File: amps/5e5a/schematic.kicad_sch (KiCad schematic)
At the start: 60 parts, among them T2 ~4.3k:8

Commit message: Fix: draw the 1 MΩ input grid leak on the jack-1 tip node, not the grid, on eight tweed/Champ sheets
Every tweed and Champ factory sheet hangs the 1 MΩ from the jack-1 tip
node (the node the jack-2 shorting contact also lands on) to ground, and
runs the 68 K stoppers from the jack tips to the grid. These eight sheets
drew the 1 MΩ on the GRID side of the stopper — one copy-pasted idiom in
four scripts and its cousins in four more; there is no shared helper, so
each script is fixed where it draws the block. The stopper is declared
DC-transparent (layout net_map.series_bridge), so the netlist sees one node
either way and verify_schematic_nets stays 40 clean; the sheet-vs-board
gate, which compares the drawings to each other, drops all twelve
MISPLACED findings (RG1/RG2 on 5e4a, 5e5a, 5f4, 5f6; R3 on 5f2a, aa764,
aa764-vibro; R1 on 5f1). 5f10's jack chain is a separate task.

Crops read: 5e4a-RG1-RG2-input.png, 5e5a-RG1-RG2-input.png,
5f4-RG1-input.png, 5f6-RG1-RG2-input.png, 5f2a-R3-input.png,
5f1-R1-input.png, aa764-R3-input.png, aa764-vibro-R3-input.png — each
prints "1 MEG." from the jack-1 tip to ground with the 68K pair to the grid.

Geometry: the four two-channel sheets hang the leak from the stopper's
jack-side pin; 5f1 drops it from the INPUT line; 5f2a and the two Champs
stand it upward off the jack-1 line because the jack-2 line runs 8–12 mm
below. Previews read cleanly. The circuit stories already say the leaks
mount at the jacks, so no prose changed.

Gates: check_schematics 40/0 (0 isolated), verify_schematic_nets 40
clean, validate/value-consistency/era-values clean, regenerate-all leaves
every other sheet byte-identical. verify_sheet_vs_board misplaced 98 -> 86.

Co-Authored-By: Claude Fable 5.1 <noreply@anthropic.com>
Claude-Session: https://claude.ai/code/session_01KBMfdh37HmCL2iWcBiL5J1
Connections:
- net INST: now also RG1.1
- net MIC: now also RG2.1
- net at R1s.2, V1A.2 (G): no longer RG1.1
- net at R2s.2, V1B.2 (G): no longer RG2.1
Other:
- moved on the sheet: RG1, RG2
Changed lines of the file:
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@@
   (wire (pts (xy 30.3 53.7) (xy 34.11 53.7))
     (stroke (width 0) (type default)))
-  (junction (at 30.3 53.7) (diameter 1.151) (color 0 0 0 0))
-  (symbol (lib_id "cx:R") (at 30.3 57.51 0) (unit 1)
+  (junction (at 22.68 53.7) (diameter 1.151) (color 0 0 0 0))
+  (symbol (lib_id "cx:R") (at 22.68 57.51 0) (unit 1)
     (in_bom yes) (on_board yes)
-    (property "Reference" "RG1" (at 32.5 54.31 0) (effects (font (size 1.27 1.27)) (justify left)))
-    (property "Value" "1M" (at 32.5 56.71 0) (effects (font (size 1.27 1.27)) (justify left))))
-  (global_label "GND" (shape input) (at 30.3 61.32 270)
+    (property "Reference" "RG1" (at 24.88 57.51 0) (effects (font (size 1.27 1.27)) (justify left)))
+    (property "Value" "1M" (at 24.88 59.91 0) (effects (font (size 1.27 1.27)) (justify left))))
+  (global_label "GND" (shape input) (at 22.68 61.32 270)
     (effects (font (size 1.27 1.27)) (justify right)))
   (wire (pts (xy 41.73 46.08) (xy 41.73 42.6))
@@
   (wire (pts (xy 30.3 87.7) (xy 34.11 87.7))
     (stroke (width 0) (type default)))
-  (junction (at 30.3 87.7) (diameter 1.151) (color 0 0 0 0))
-  (symbol (lib_id "cx:R") (at 30.3 91.51 0) (unit 1)
+  (junction (at 22.68 87.7) (diameter 1.151) (color 0 0 0 0))
+  (symbol (lib_id "cx:R") (at 22.68 91.51 0) (unit 1)
     (in_bom yes) (on_board yes)
-    (property "Reference" "RG2" (at 32.5 88.31 0) (effects (font (size 1.27 1.27)) (justify left)))
-    (property "Value" "1M" (at 32.5 90.71 0) (effects (font (size 1.27 1.27)) (justify left))))
-  (global_label "GND" (shape input) (at 30.3 95.32 270)
+    (property "Reference" "RG2" (at 24.88 91.51 0) (effects (font (size 1.27 1.27)) (justify left)))
+    (property "Value" "1M" (at 24.88 93.91 0) (effects (font (size 1.27 1.27)) (justify left))))
+  (global_label "GND" (shape input) (at 22.68 95.32 270)
     (effects (font (size 1.27 1.27)) (justify right)))
   (wire (pts (xy 41.73 80.08) (xy 41.73 76.6))

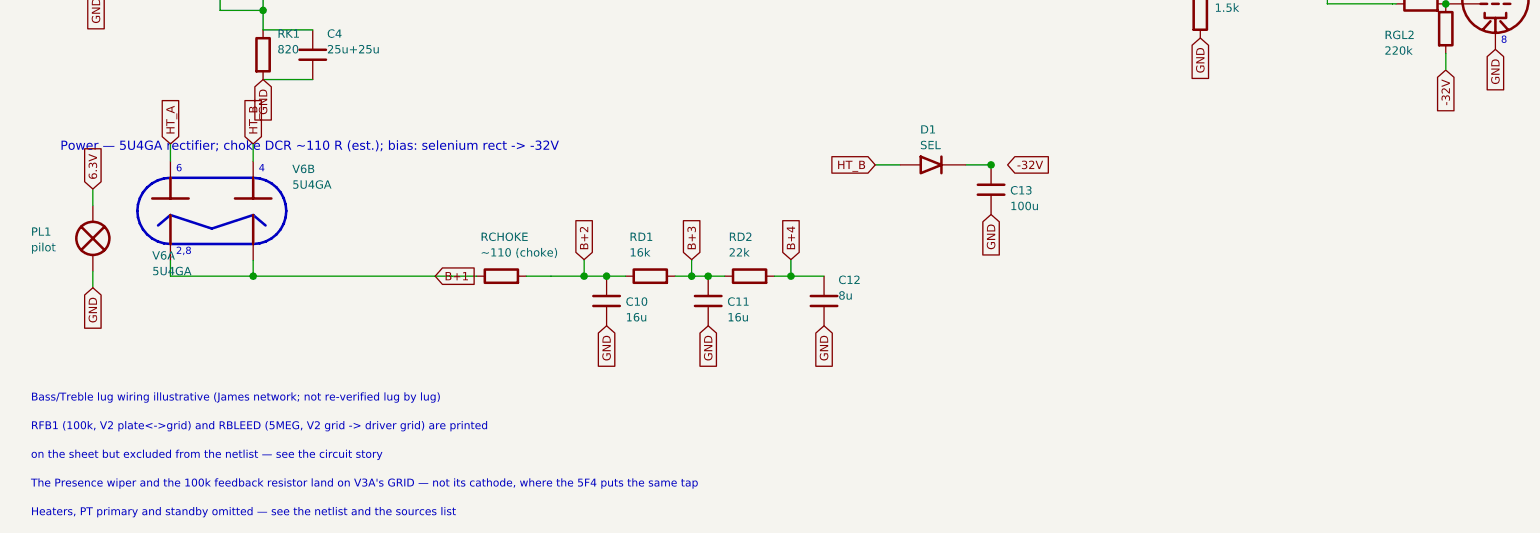
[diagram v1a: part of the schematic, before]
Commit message: Fix: feed the tweed bias rectifiers from the transformer's bias tap, not a rectifier plate (5E4-A, 5E5-A, 5F4, 5G9)
The 8087-family power transformer brings out a BIAS TAP on the HT winding,
between one end and the centre tap — the layouts letter that lead RED-BLUE
— and every fixed-bias tweed factory sheet draws the bias rectifier from
that fourth winding terminal. These four sheets drew it from a rectifier
plate (the HT_B label). The boards carry the same mistake, which is why the
sheet-vs-board gate could not see it; the source read did.

cx:PT gains an OPTIONAL pin 6, HT_TAP, between HT_A and the centre tap.
`s.pt(..., tap=True)` asks for it, and only that sheet's embedded library
carries the pin (lib_text(pt_tap=...)), so every sheet that does not wire
it is byte-identical — proved by the regenerate-all diff below. The
contract tables (SYM_EXTENTS/SYM_PINS) are built with the pin so the lint
and the wire-cutting know it; the tap lies inside the symbol's box, so no
extent moves.

- 5g9: T1 8160 drawn with the tap (moved 8 mm left for the label), the
  selenium rectifier's AC side on HT_TAP (crop 5g9-D1-schem.png: the
  rectifier + runs straight to a winding terminal between the 300 V AC end
  and the centre tap; layout: a separate lead to SEL. RECT. +).
- 5e4a, 5f4: these sheets drew no PT at all, so a T1 is added (MAINS labels
  on the primary, HT_A / HT_TAP / centre tap / HT_B on the secondary, the
  same idiom the 5G9 uses), the 18k / 6800 bias feed taken from HT_TAP,
  and T1 added to bom.yaml (crops 5e4a-D1-schem.png, 5f4-D1-schem.png:
  the series resistor from a winding terminal between the top end and the
  centre tap; 5e4a-D1-layout.png: RED-BLUE lead to the selenium +).
- 5e5a: T1 added the same way; the bias row now carries the factory's 10 K
  in series from the tap into the cell and the 56 K bleeder across the
  100 µF can (crop 5e5a-D1-schem.png), both added to bom.yaml (RB1, RB2)
  — the board places neither, so they report SHEET-ONLY until it doe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
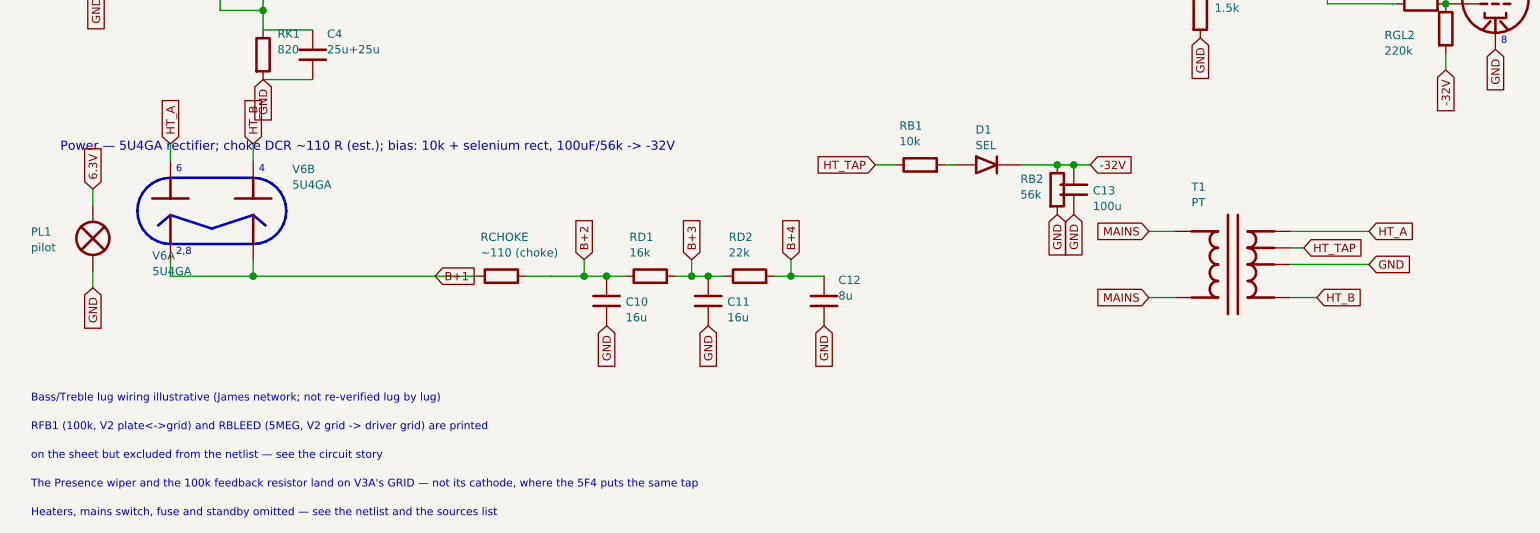
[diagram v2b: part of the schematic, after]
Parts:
- added RB1: 10k, symbol cx:R
- added RB2: 56k, symbol cx:R
- added T1: PT, symbol cx:PT
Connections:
- net -32V: now also C13.1, D1.2 (K), RB2.1
- net GND: now also RB2.2, T1.4 (HT_CT)
- net HT_A: now also T1.3 (HT_A)
- net HT_B: now also T1.5 (HT_B); no longer D1.1 (A)
- new net: D1.1 (A), RB1.2
- new net HT_TAP: RB1.1, T1.6 (HT_TAP)
- new net MAINS: T1.1 (PRI_1), T1.2 (PRI_2)
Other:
- note added: "Heaters, mains switch, fuse and standby omitted — see the netlist and the sources list"
- note added: "Power — 5U4GA rectifier; choke DCR ~110 R (est.); bias: 10k + selenium rect, 100uF/56k -> -32V"
- note removed: "Heaters, PT primary and standby omitted — see the netlist and the sources list"
- note removed: "Power — 5U4GA rectifier; choke DCR ~110 R (est.); bias: selenium rect -> -32V"
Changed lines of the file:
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@@
   (text "Extra 8-ohm speaker jack (parallel) omitted — annotation only" (at 242.2 83.7 0)
     (effects (font (size 1 1)) (justify left)))
-  (text "Power — 5U4GA rectifier; choke DCR ~110 R (est.); bias: selenium rect -> -32V" (at 17.2 119.7 0)
+  (text "Power — 5U4GA rectifier; choke DCR ~110 R (est.); bias: 10k + selenium rect, 100uF/56k -> -32V" (at 17.2 119.7 0)
     (effects (font (size 1.4 1.4)) (justify left)))
   (symbol (lib_id "cx:LAMP") (at 22.2 133.7 0) (unit 1)
@@
   (global_label "GND" (shape input) (at 134.44 147.12 270)
     (effects (font (size 1.27 1.27)) (justify right)))
-  (global_label "HT_B" (shape input) (at 142.3 122.42 180)
-    (effects (font (size 1.27 1.27)) (justify right)))
-  (wire (pts (xy 142.3 122.42) (xy 146.11 122.42))
-    (stroke (width 0) (type default)))
-  (symbol (lib_id "cx:DIODE_SS") (at 151.19 122.42 0) (unit 1)
-    (in_bom yes) (on_board yes)
-    (property "Reference" "D1" (at 149.19 117.02 0) (effects (font (size 1.27 1.27)) (justify left)))
-    (property "Value" "SEL" (at 149.19 119.42 0) (effects (font (size 1.27 1.27)) (justify left))))
-  (wire (pts (xy 156.27 122.42) (xy 160.08 122.42))
-    (stroke (width 0) (type default)))
-  (junction (at 160.08 122.42) (diameter 1.151) (color 0 0 0 0))
-  (symbol (lib_id "cx:C") (at 160.08 126.23 0) (unit 1)
-    (in_bom yes) (on_board yes)
-    (property "Reference" "C13" (at 163.012 126.368 0) (effects (font (size 1.27 1.27)) (justify left)))
-    (property "Value" "100u" (at 163.012 128.768 0) (effects (font (size 1.27 1.27)) (justify left))))
-  (global_label "GND" (shape input) (at 160.08 130.04 270)
-    (effects (font (size 1.27 1.27)) (justify right)))
-  (global_label "-32V" (shape input) (at 162.62 122.42 0)
+  (global_label "HT_TAP" (shape input) (at 142.3 122.42 180)
+    (effects (font (size 1.27 1.27)) (justify right)))
+  (symbol (lib_id "cx:R") (at 149.2 122.42 90) (unit 1)
+    (in_bom yes) (on_board yes)
+    (property "Reference" "RB1" (at 146 116.42 270) (effects (font (size 1.27 1.27)) (justify left)))
+    (property "Value" "10k" (at 146 118.82 270) (effects (font (size 1.27 1.27)) (justify left))))
+  (wire (pts (xy 142.3 122.42) (xy 145.39 122.42))
+    (stroke (width 0) (type default)))
+  (wire (pts (xy 153.01 122.42) (xy 154.62 122.42))
+    (stroke (width 0) (type default)))
+  (symbol (lib_id "cx:DIODE_SS") (at 159.7 122.42 0) (unit 1)
+    (in_bom yes) (on_board yes)
+    (property "Reference" "D1" (at 157.7 117.02 0) (effects (font (size 1.27 1.27)) (justify left)))
+    (property "Value" "SEL" (at 157.7 119.42 0) (effects (font (size 1.27 1.27)) (justify left))))
+  (wire (pts (xy 164.78 122.42) (xy 170.24 122.42))
+    (stroke (width 0) (type default)))
+  (wire (pts (xy 170.24 122.42) (xy 172.78 122.42))
+    (stroke (width 0) (type default)))
+  (wire (pts (xy 172.78 122.42) (xy 175.32 122.42))
+    (stroke (width 0) (type default)))
+  (junction (at 170.24 122.42) (diameter 1.151) (color 0 0 0 0))
+  (symbol (lib_id "cx:R") (at 170.24 126.23 0) (unit 1)
+    (in_bom yes) (on_board yes)
+    (property "Reference" "RB2" (at 164.575 124.59 0) (effects (font (size 1.27 1.27)) (justify left)))
+    (property "Value" "56k" (at 164.575 126.99 0) (effects (font (size 1.27 1.27)) (justify left))))
+  (global_label "GND" (shape input) (at 170.24 130.04 270)
+    (effects (font (size 1.27 1.27)) (justify right)))
+  (junction (at 172.78 122.42) (diameter 1.151) (color 0 0 0 0))
+  (symbol (lib_id "cx:C") (at 172.78 126.23 0) (unit 1)
+    (in_bom yes) (on_board yes)
+    (property "Reference" "C13" (at 175.712 126.368 0) (effects (font (size 1.27 1.27)) (justify left)))
+    (property "Value" "100u" (at 175.712 128.768 0) (effects (font (size 1.27 1.27)) (justify left))))
+  (global_label "GND" (shape input) (at 172.78 130.04 270)
+    (effects (font (size 1.27 1.27)) (justify right)))
+  (global_label "-32V" (shape input) (at 175.32 122.42 0)
+    (effects (font (size 1.27 1.27)) (justify left)))
+  (symbol (lib_id "cx:PT") (at 197.2 137.7 0) (unit 1)
+    (in_bom yes) (on_board yes)
+    (property "Reference" "T1" (at 190.85 125.8 0) (effects (font (size 1.27 1.27)) (justify left)))
+    (property "Value" "PT" (at 190.85 128.2 0) (effects (font (size 1.27 1.27)) (justify left))))
+  (wire (pts (xy 188.31 132.62) (xy 184.31 132.62))
+    (stroke (width 0) (type default)))
+  (global_label "MAINS" (shape input) (at 184.31 132.62 180)
+    (effects (font (size 1.27 1.27)) (justify right)))
+  (wire (pts (xy 188.31 142.78) (xy 184.31 142.78))
+    (stroke (width 0) (type default)))
+  (global_label "MAINS" (shape input) (at 184.31 142.78 180)
+    (effects (font (size 1.27 1.27)) (justify right)))
+  (wire (pts (xy 206.09 132.62) (xy 218.09 132.62))
+    (stroke (width 0) (type default)))
+  (global_label "HT_A" (shape input) (at 218.09 132.62 0)
+    (effects (font (size 1.27 1.27)) (justify left)))
+  (wire (pts (xy 206.09 135.16) (xy 208.09 135.16))
+    (stroke (width 0) (type default)))
+  (global_label "HT_TAP" (shape input) (at 208.09 135.16 0)
+    (effects (font (size 1.27 1.27)) (justify left)))
+  (wire (pts (xy 206.09 137.7) (xy 218.09 137.7))
+    (stroke (width 0) (type default)))
+  (global_label "GND" (shape input) (at 218.09 137.7 0)
+    (effects (font (size 1.27 1.27)) (justify left)))
+  (wire (pts (xy 206.09 142.78) (xy 210.09 142.78))
+    (stroke (width 0) (type default)))
+  (global_label "HT_B" (shape input) (at 210.09 142.78 0)
     (effects (font (size 1.27 1.27)) (justify left)))
   (polyline (pts (xy 46.81 124.4) (xy 47.801 124.498) (xy 48.754 124.787) (xy 49.632 125.256) (xy 50.402 125.888) (xy 51.034 126.658) (xy 51.503 127.536) (xy 51.792 128.489) (xy 51.89 129.48) (xy 51.792 130.471) (xy 51.503 131.424) (xy 51.034 132.302) (xy 50.402 133.072) (xy 49.632 133.704) (xy 48.754 134.173) (xy 47.801 134.462) (xy 46.81 134.56) (xy 34.11 134.56) (xy 33.119 134.462) (xy 32.166 134.173) (xy 31.288 133.704) (xy 30.518 133.072) (xy 29.886 132.302) (xy 29.417 131.424) (xy 29.128 130.471) (xy 29.03 129.48) (xy 29.128 128.489) (xy 29.417 127.536) (xy 29.886 126.658) (xy 30.518 125.888) (xy 31.288 125.256) (xy 32.166 124.787) (xy 33.119 124.498) (xy 34.11 124.4) (xy 46.81 124.4))
@@
   (text "The Presence wiper and the 100k feedback resistor land on V3A's GRID — not its cathode, where the 5F4 puts the same tap" (at 12.7 171.478 0)
     (effects (font (size 1.2 1.2)) (justify left)))
-  (text "Heaters, PT primary and standby omitted — see the netlist and the sources list" (at 12.7 175.878 0)
+  (text "Heaters, mains switch, fuse and standby omitted — see the netlist and the sources list" (at 12.7 175.878 0)
     (effects (font (size 1.2 1.2)) (justify left)))
   (sheet_instances (path "/" (page "1")))

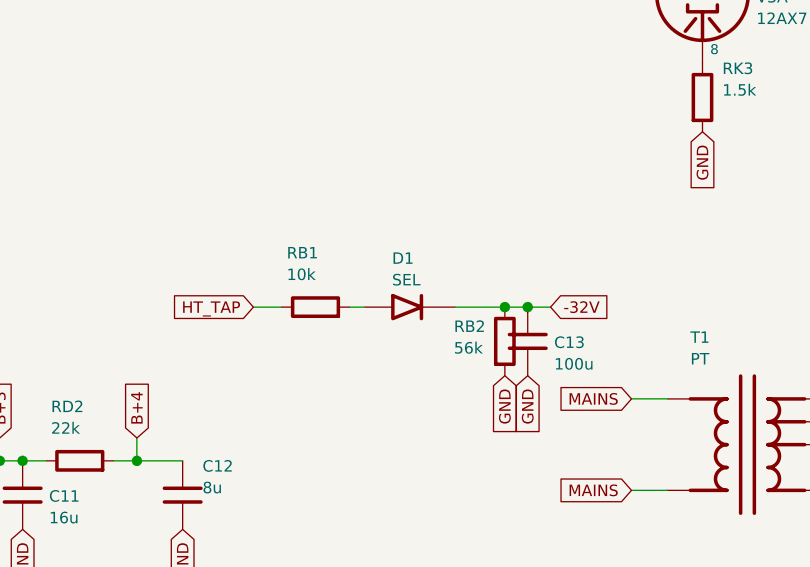
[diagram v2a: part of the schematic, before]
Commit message: Fix: 17 bias rectifiers and six HT diodes drawn backwards; the 6G6-B and 6G4 bias rows as their drawings show; AA1164 V4 units
Rectifier polarity has no gate. The netlists model every supply as an ideal
source, the sheet-vs-board check treats a two-terminal part as unordered, and
the boards' `cathode:` fields were copied from the sheets. Measured over all
68 diodes on 40 sheets: 18 negative-bias rectifiers had the cathode on the
negative node (a diode that way round would charge the node POSITIVE), and all
six 6G6-B HT diodes pointed away from B+. The printed negative bias on each of
those sheets falsifies the drawn orientation; the nine bias rectifiers already
right (AA1164, AA864, AB165, B15N, DR103, JTM100, M1959, M2204, 6G6-B) show
the idiom. Flipped: 5E4-A, 5E5-A, 5E6-A, 5F10, 5F4, 5F6, 5F6-A, 5F8-A, 5G9,
6G2, 6G3, 6G4, 6G5, AA964, AB763, AB763 Super, AB763 Twin, JTM45 (the
M1987's is with the Marshall board repair) and the 6G6-B's DR1-DR6. The
5F8-A board, which had copied its sheet, has the band moved to the tap side;
the other boards' bands are with the board-repair wave. A gate is next.

6G6-B bias. E-FB (6431x3364): the 1K 1W rises from TR1's SECOND secondary
terminal, a bias tap between the upper HT end and the grounded centre tap,
to the diode's + end. The sheet fed the diode from the HT end with the 1K
after it. T1 now carries its tap pin and the row reads tap -> 1K -> diode ->
-54 V. (The triage had read "HT end"; the native crop shows the tap.)

6G4 bias. A-FJ, read natively: tap -> rectifier -> 8 uF -> 10K -> the -55 V
node, which carries a second 8 uF and the 56K to ground as a bleeder. The
sheet fed the rectifier from an HT end, drew the 56K in series and carried
one capacitor. CBIAS2 joins the parts list, and RBIAS1's role now says
bleeder.

AA1164 V4. The K-FD sheet prints the phase inverter 7/6/8 and the tremolo
oscillator 2/1/3 (5554x4346); the sheet had them the other way round.

Gates: check_schematics 40/0 (+selftest), verify_schematic_nets 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
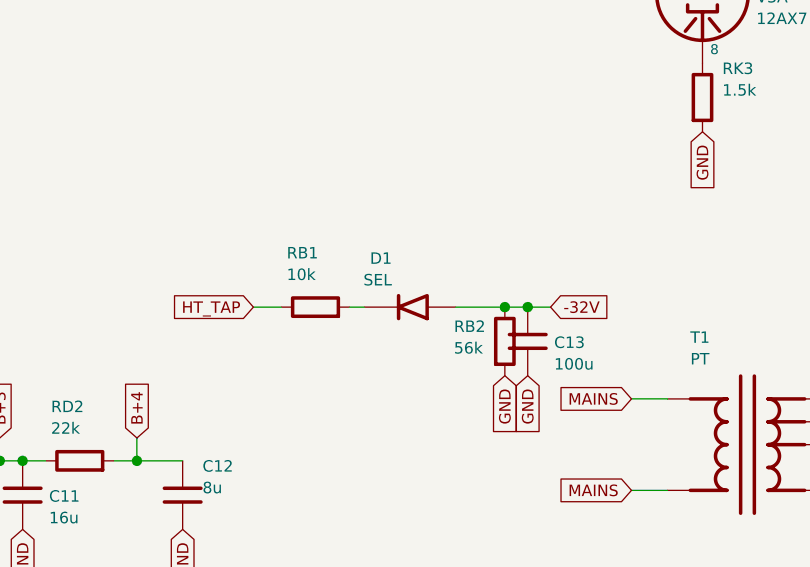
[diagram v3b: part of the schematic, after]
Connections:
- net -32V: now also D1.1 (A); no longer D1.2 (K)
- net at RB1.2: now also D1.2 (K); no longer D1.1 (A)
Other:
- moved on the sheet: D1
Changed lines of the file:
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@@
   (wire (pts (xy 153.01 122.42) (xy 154.62 122.42))
     (stroke (width 0) (type default)))
-  (symbol (lib_id "cx:DIODE_SS") (at 159.7 122.42 0) (unit 1)
+  (symbol (lib_id "cx:DIODE_SS") (at 159.7 122.42 180) (unit 1)
     (in_bom yes) (on_board yes)
     (property "Reference" "D1" (at 157.7 117.02 0) (effects (font (size 1.27 1.27)) (justify left)))
